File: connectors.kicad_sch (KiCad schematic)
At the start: 3 parts, among them J1 Conn_02x04_Odd_Even, J2 SMA, J3 SMA

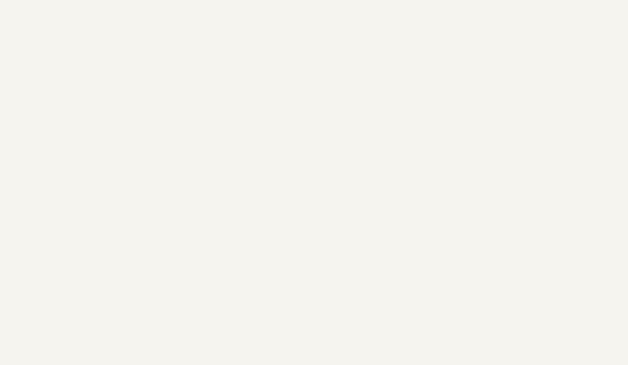
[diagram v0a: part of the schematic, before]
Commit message: switch to 4-layer 1.6mm PCB stackup from JLCPCB
- By recommendation of reviewers, use a 4-layer 1.6 PCB stackup from
JLCPCB that gives 0.6 mm 50 ohm CPWG traces on the top layer.

- Use an SMA connector with a thin pin for the RF output.

- Remove 51 ohm resistor loading the ADF4518 PCB. This is believed
to be a mistake in the evaluation board schematic.

- Add M2 mounting holes to the board corners.

- Connect NC pins of HMC391 to GND as in the evaluation board.

Signed-off-by: Daniel Estévez <daniel@destevez.net>
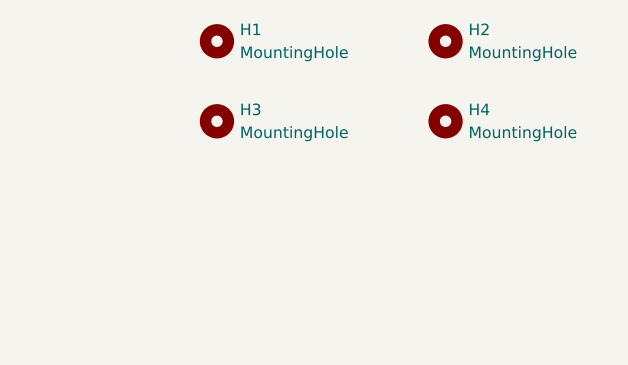
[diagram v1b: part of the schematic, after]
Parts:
- added H1, H2, H3, H4: MountingHole, MountingHole:MountingHole_2.2mm_M2, symbol Mechanical:MountingHole
- J2: footprint ADF4158_HMC391_PCB:WRL-23187 -> ADF4158_HMC391_PCB:2484637-1; Digikey Part Number 1568-WRL-23187-ND -> 343-2484637-1-ND

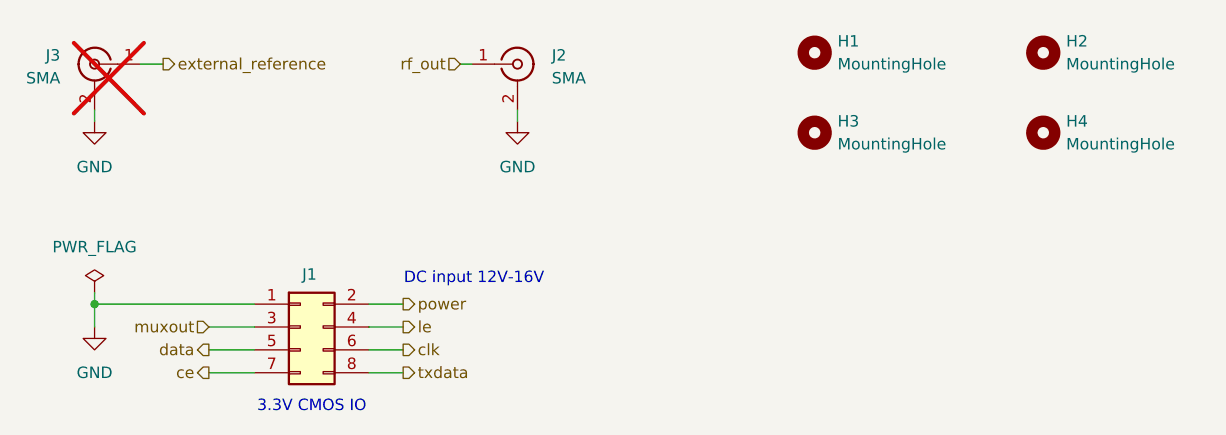
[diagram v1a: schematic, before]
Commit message: add plating to mounting holes
Signed-off-by: Daniel Estévez <daniel@destevez.net>
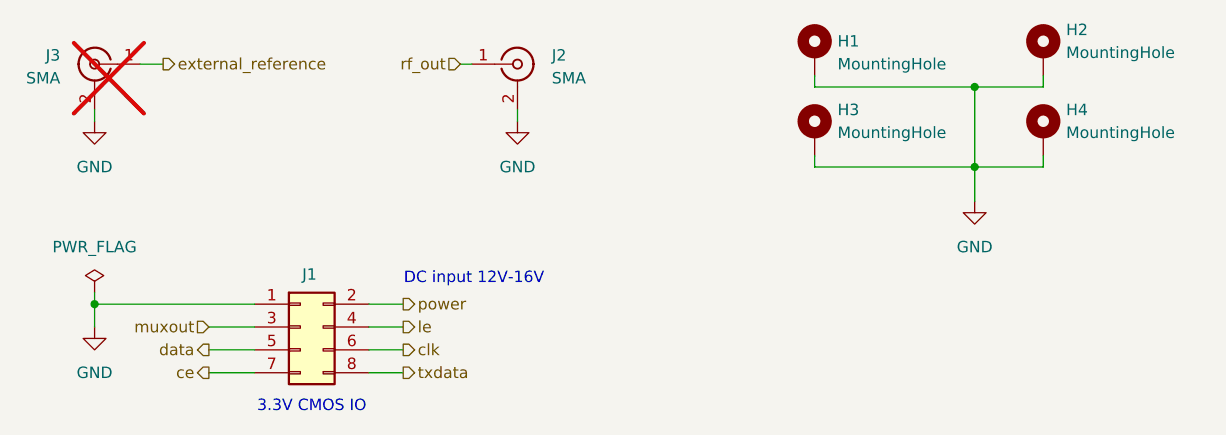
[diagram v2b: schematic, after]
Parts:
- H1, H2, H3, H4: footprint MountingHole:MountingHole_2.2mm_M2 -> MountingHole:MountingHole_2.2mm_M2_Pad; symbol Mechanical:MountingHole -> Mechanical:MountingHole_Pad
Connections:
- net GND: now also H1.1, H2.1, H3.1, H4.1
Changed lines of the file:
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@@
+	)
+	(junction
+		(at 218.44 82.55)
+		(diameter 0)
+		(color 0 0 0 0)
 	)
 	(junction
@@
 		(color 0 0 0 0)
 	)
+	(junction
+		(at 218.44 91.44)
+		(diameter 0)
+		(color 0 0 0 0)
+	)
 	(wire
 		(pts
@@
 	(wire
 		(pts
+			(xy 218.44 82.55) (xy 226.06 82.55)
+		)
+		(stroke
+			(width 0)
+			(type default)
+		)
+	)
+	(wire
+		(pts
 			(xy 133.35 109.22) (xy 138.43 109.22)
 		)
@@
 	(wire
 		(pts
+			(xy 200.66 91.44) (xy 218.44 91.44)
+		)
+		(stroke
+			(width 0)
+			(type default)
+		)
+	)
+	(wire
+		(pts
 			(xy 133.35 114.3) (xy 138.43 114.3)
 		)
@@
 	(wire
 		(pts
+			(xy 226.06 90.17) (xy 226.06 91.44)
+		)
+		(stroke
+			(width 0)
+			(type default)
+		)
+	)
+	(wire
+		(pts
+			(xy 200.66 82.55) (xy 218.44 82.55)
+		)
+		(stroke
+			(width 0)
+			(type default)
+		)
+	)
+	(wire
+		(pts
 			(xy 125.73 80.01) (xy 128.27 80.01)
 		)
@@
 	(wire
 		(pts
+			(xy 218.44 82.55) (xy 218.44 91.44)
+		)
+		(stroke
+			(width 0)
+			(type default)
+		)
+	)
+	(wire
+		(pts
 			(xy 151.13 111.76) (xy 154.94 111.76)
 		)
@@
 	(wire
 		(pts
+			(xy 200.66 81.28) (xy 200.66 82.55)
+		)
+		(stroke
+			(width 0)
+			(type default)
+		)
+	)
+	(wire
+		(pts
 			(xy 133.35 111.76) (xy 138.43 111.76)
+		)
+		(stroke
+			(width 0)
+			(type default)
+		)
+	)
+	(wire
+		(pts
+			(xy 226.06 91.44) (xy 218.44 91.44)
+		)
+		(stroke
+			(width 0)
+			(type default)
+		)
+	)
+	(wire
+		(pts
+			(xy 200.66 90.17) (xy 200.66 91.44)
+		)
+		(stroke
+			(width 0)
+			(type default)
+		)
+	)
+	(wire
+		(pts
+			(xy 226.06 81.28) (xy 226.06 82.55)
+		)
+		(stroke
+			(width 0)
+			(type default)
+		)
+	)
+	(wire
+		(pts
+			(xy 218.44 91.44) (xy 218.44 95.25)
 		)
 		(stroke
@@
 	)
 	(symbol
-		(lib_id "Mechanical:MountingHole")
+		(lib_id "Mechanical:MountingHole_Pad")
 		(at 226.06 78.74 0)
 		(unit 1)
@@
 		(fields_autoplaced yes)
 		(property "Reference" "H2"
-			(at 228.6 77.4699 0)
+			(at 228.6 76.1999 0)
 			(effects
 				(font
@@
 		)
 		(property "Value" "MountingHole"
-			(at 228.6 80.0099 0)
+			(at 228.6 78.7399 0)
 			(effects
 				(font
@@
 			)
 		)
-		(property "Footprint" "MountingHole:MountingHole_2.2mm_M2"
+		(property "Footprint" "MountingHole:MountingHole_2.2mm_M2_Pad"
 			(at 226.06 78.74 0)
 			(effects
@@
 			)
 		)
-		(property "Description" "Mounting Hole without connection"
+		(property "Description" "Mounting Hole with connection"
 			(at 226.06 78.74 0)
 			(effects
@@
 				(hide yes)
 			)
+		)
+		(pin "1"
 		)
 		(instances
@@
 	)
 	(symbol
-		(lib_id "Mechanical:MountingHole")
+		(lib_id "power:GND")
+		(at 218.44 95.25 0)
+		(unit 1)
+		(exclude_from_sim no)
+		(in_bom yes)
+		(on_board yes)
+		(dnp no)
+		(fields_autoplaced yes)
+		(property "Reference" "#PWR024"
+			(at 218.44 101.6 0)
+			(effects
+				(font
+					(size 1.27 1.27)
+				)
+				(hide yes)
+			)
+		)
+		(property "Value" "GND"
+			(at 218.44 100.33 0)
+			(effects
+				(font
+					(size 1.27 1.27)
+				)
+			)
+		)
+		(property "Footprint" ""
+			(at 218.44 95.25 0)
+			(effects
+				(font
+					(size 1.27 1.27)
+				)
+				(hide yes)
+			)
+		)
+		(property "Datasheet" ""
+			(at 218.44 95.25 0)
+			(effects
+				(font
+					(size 1.27 1.27)
+				)
+				(hide yes)
+			)
+		)
+		(property "Description" "Power symbol creates a global label with name \"GND\" , ground"
+			(at 218.44 95.25 0)
+			(effects
+				(font
+					(size 1.27 1.27)
+				)
+				(hide yes)
+			)
+		)
+		(pin "1"
+		)
+		(instances
+			(project ""
+				(path "/3d5adadc-a9f6-49bf-a77d-66e214ec66a0/43667435-3031-489c-af69-4725b093739b"
+					(reference "#PWR024")
+					(unit 1)
+				)
+			)
+		)
+	)
+	(symbol
+		(lib_id "Mechanical:MountingHole_Pad")
 		(at 200.66 87.63 0)
 		(unit 1)
@@
 		(fields_autoplaced yes)
 		(property "Reference" "H3"
-			(at 203.2 86.3599 0)
+			(at 203.2 85.0899 0)
 			(effects
 				(font
@@
 		)
 		(property "Value" "MountingHole"
-			(at 203.2 88.8999 0)
+			(at 203.2 87.6299 0)
 			(effects
 				(font
@@
 			)
 		)
-		(property "Footprint" "MountingHole:MountingHole_2.2mm_M2"
+		(property "Footprint" "MountingHole:MountingHole_2.2mm_M2_Pad"
 			(at 200.66 87.63 0)
 			(effects
@@
 			)
 		)
-		(property "Description" "Mounting Hole without connection"
+		(property "Description" "Mounting Hole with connection"
 			(at 200.66 87.63 0)
 			(effects
@@
 				(hide yes)
 			)
+		)
+		(pin "1"
 		)
 		(instances
@@
 	)
 	(symbol
-		(lib_id "Mechanical:MountingHole")
+		(lib_id "Mechanical:MountingHole_Pad")
 		(at 200.66 78.74 0)
 		(unit 1)
@@
 		(on_board yes)
 		(dnp no)
-		(fields_autoplaced yes)
 		(property "Reference" "H1"
 			(at 203.2 77.4699 0)
@@
 			)
 		)
-		(property "Footprint" "MountingHole:MountingHole_2.2mm_M2"
+		(property "Footprint" "MountingHole:MountingHole_2.2mm_M2_Pad"
 			(at 200.66 78.74 0)
 			(effects
@@
 			)
 		)
-		(property "Description" "Mounting Hole without connection"
+		(property "Description" "Mounting Hole with connection"
 			(at 200.66 78.74 0)
 			(effects
@@
 				(hide yes)
 			)
+		)
+		(pin "1"
 		)
 		(instances
@@
 	)
 	(symbol
-		(lib_id "Mechanical:MountingHole")
+		(lib_id "Mechanical:MountingHole_Pad")
 		(at 226.06 87.63 0)
 		(unit 1)
@@
 		(fields_autoplaced yes)
 		(property "Reference" "H4"
-			(at 228.6 86.3599 0)
+			(at 228.6 85.0899 0)
 			(effects
 				(font
@@
 		)
 		(property "Value" "MountingHole"
-			(at 228.6 88.8999 0)
+			(at 228.6 87.6299 0)
 			(effects
 				(font
@@
 			)
 		)
-		(property "Footprint" "MountingHole:MountingHole_2.2mm_M2"
+		(property "Footprint" "MountingHole:MountingHole_2.2mm_M2_Pad"
 			(at 226.06 87.63 0)
 			(effects
@@
 			)
 		)
-		(property "Description" "Mounting Hole without connection"
+		(property "Description" "Mounting Hole with connection"
 			(at 226.06 87.63 0)
 			(effects
@@
 			)
 		)
+		(pin "1"
+		)
 		(instances
